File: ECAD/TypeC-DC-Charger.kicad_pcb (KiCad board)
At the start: 4 copper layers, 48 x 56 mm, 91 parts, among them CON1 XT60-PT-MALE, J1 USB_C_SOCKET_RA_SMD, Q1 CSD18543Q3A, Q2 CSD18543Q3A, Q3 CSD17551Q3A, Q4 CSD17551Q3A, Q5 CSD17579Q3A, Q6 CSD17579Q3A, Q7 CSD17579Q3A, Q8 BC857B, Q9 IRFR9024NTRPBF, U1 LM5175RHF, U2 TPS25741, U3 TPS2514

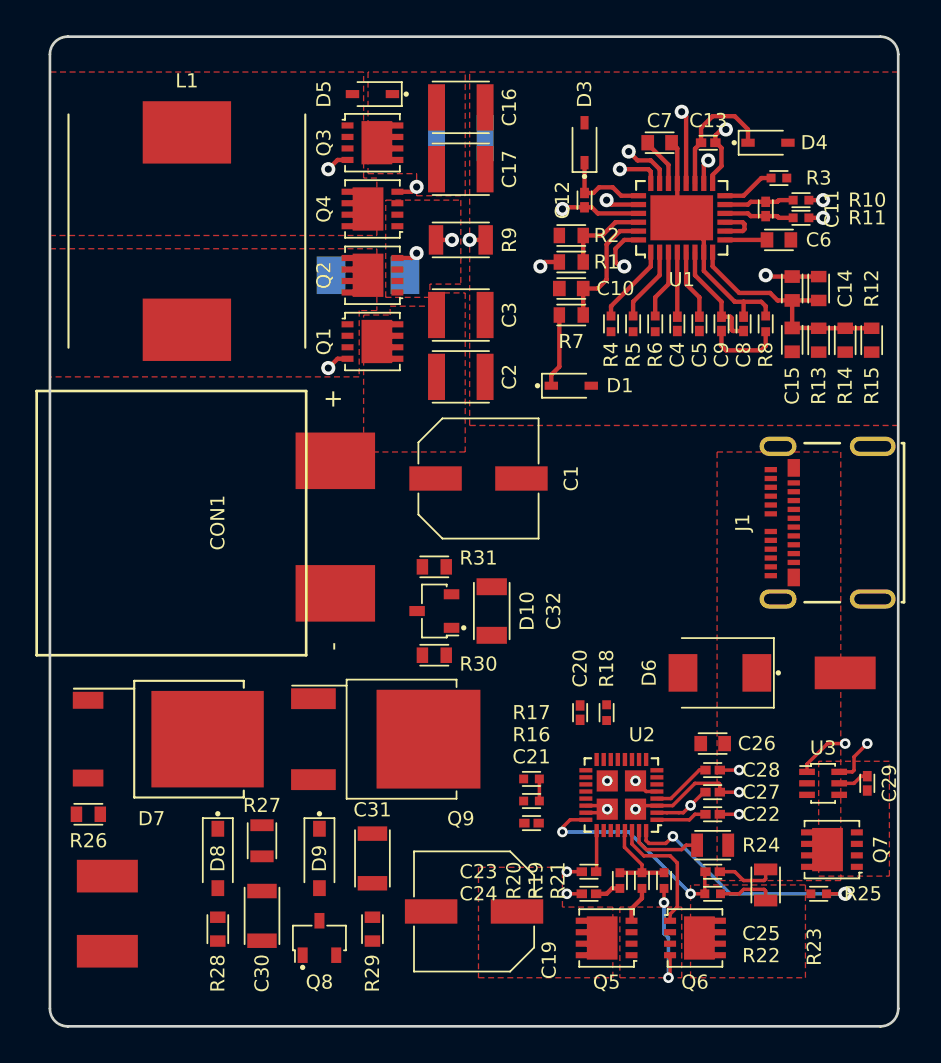
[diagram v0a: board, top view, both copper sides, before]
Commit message: Added dip switch selection to charge settings. PCB placement improvements. Added 3mm led placeholder for indicator led.
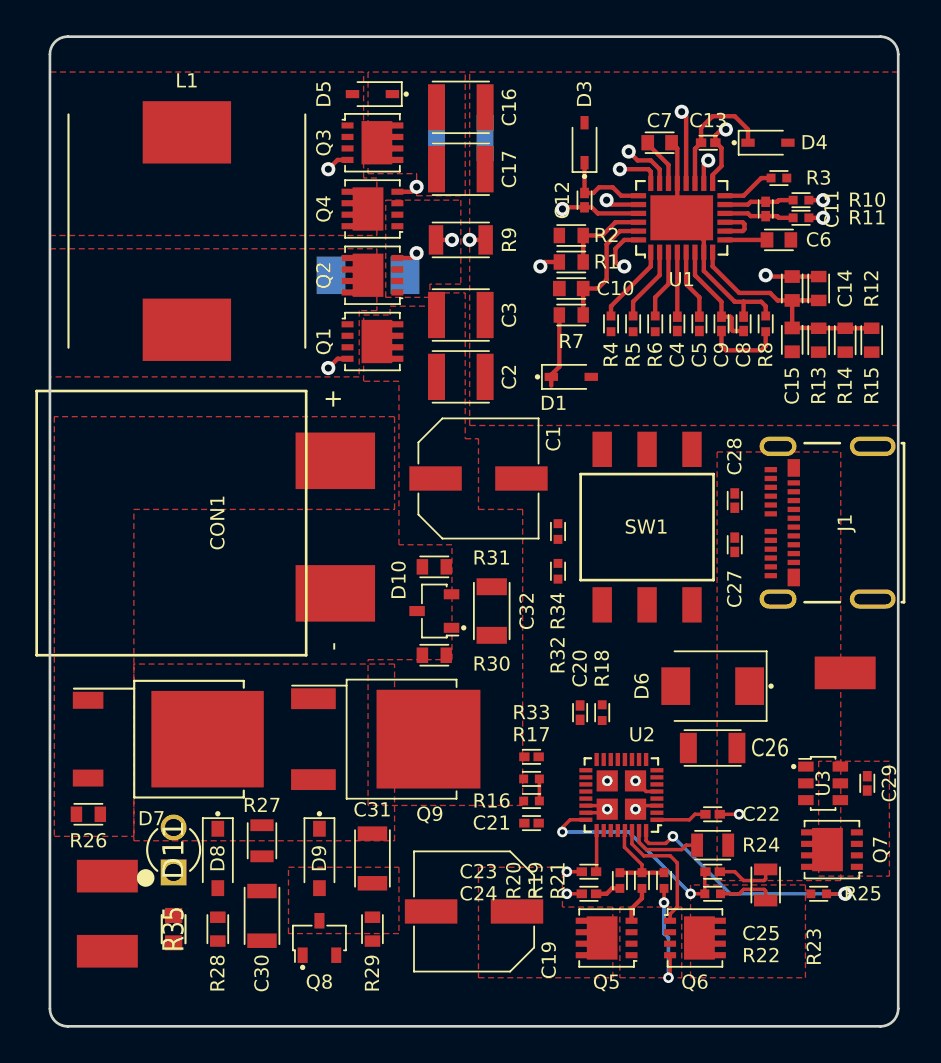
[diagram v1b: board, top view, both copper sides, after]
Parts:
- added D11: LED_RED_3MM_PTH, Applidyne_LED:LEDRD254W40D300H700, F.Cu at (107.0, 96.0)
- added R32: 220K_1005M, Applidyne_Resistor:RESC1005X40L, F.Cu at (128.8, 80.2)
- added R33: 0R_1005M, Applidyne_Capacitor:CAPC1005X60L, F.Cu at (127.2, 90.8)
- added R34: 220K_1005M, Applidyne_Resistor:RESC1005X40L, F.Cu at (128.8, 78.0)
- added R35: 1K00_1608M, Applidyne_Resistor:RESC1608X50N, F.Cu at (107.0, 100.5)
- added SW1: 2.54mm_3xSPST_SMD, Applidyne_Switch:MCEMR-03-T, F.Cu at (131.2, 77.8)
- C26: value 6.8UF_X7R_1608M -> 6.8UF_X7R_3216M; footprint Applidyne_Capacitor:CAPC1608X90L -> Applidyne_Capacitor:CAPC3216X135L
- U3: footprint Applidyne_SOT:SOT23-6P65_210X100L36X22L -> Applidyne_SOT:SOT95P240X110-6L16L
- moved C28 15.3 mm to (138.8, 76.2), turned to 90 degrees
- moved C27 14.1 mm to (138.8, 78.8), turned to 270 degrees
- moved D6 0.85 mm to (137.5, 86.8)
- moved D1 0.50 mm to (129.5, 69.2)
- moved C26 0.25 mm to (137.5, 90.2)
- moved R18 0.25 mm to (131.2, 88.2)
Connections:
- net GDPG renamed Net-(U2-Pad27)
- net Net-(CON1-Pad2) renamed /Connectors/RAW_BATT
- net Net-(R18-Pad2) renamed /USBC Controller/PSEL
- U2 pad 10: /USBC Controller/DVDD -> /USBC Controller/EN12V
- U2 pad 19: /USBC Controller/DVDD -> Net-(R33-Pad2)
- U2 pad 6: /USBC Controller/DVDD -> /USBC Controller/HIPWR
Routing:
- net GND: track 30.3 -> 23.6 mm, vias 11 -> 9
- net CC2: track 3.42 -> 0.00 mm
- net CC1: track 3.23 -> 0.00 mm, vias 1 -> 0
- net D+: track 3.08 -> 0.00 mm, vias 1 -> 0
- net D-: track 2.70 -> 0.00 mm, vias 1 -> 0
- net /Connectors/5V: track 1.76 -> 0.00 mm
- added copper zone on F.Cu, net /Connectors/RAW_BATT
- added copper zone on F.Cu, net Net-(C31-Pad1)
- added copper zone on F.Cu, net Net-(C31-Pad2)

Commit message: Silkscreen text for dip switches, part placement improvements.
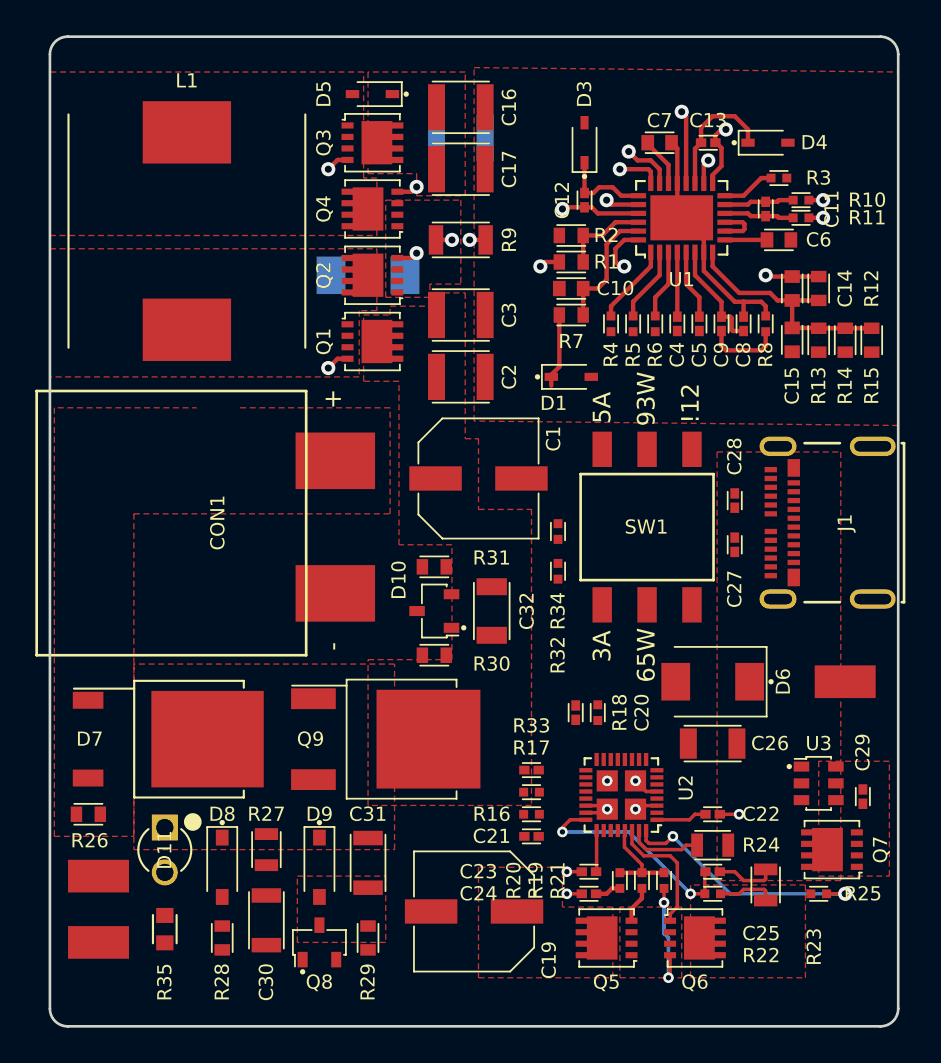
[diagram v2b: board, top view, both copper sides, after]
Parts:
- moved TEST2 4.28 mm to (102.8, 97.5)
- moved TEST5 3.78 mm to (102.8, 101.2)
- moved C29 0.79 mm to (146.0, 93.0)
- moved C21 0.75 mm to (127.2, 95.2)
- moved R16 0.75 mm to (127.2, 94.0)
- moved R17 0.75 mm to (127.2, 92.8)
- moved R33 0.75 mm to (127.2, 91.5)
- moved D8 0.56 mm to (109.8, 97.0)
- moved R27 0.56 mm to (112.2, 96.0)
- moved R28 0.56 mm to (109.8, 101.0)
- moved R29 0.56 mm to (118.0, 101.0)
- moved D11 0.50 mm to (106.5, 96.0), turned to 270 degrees
- moved D9 0.50 mm to (115.2, 97.0)
- moved R35 0.50 mm to (106.5, 100.5)
- moved TEST3 0.50 mm to (145.0, 86.5)
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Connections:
- SW1 pad 3: /USBC Controller/EN12V -> /USBC Controller/PSEL
- SW1 pad 4: GND -> /USBC Controller/DVDD
- SW1 pad 5: /USBC Controller/PSEL -> /USBC Controller/EN12V
- SW1 pad 6: /USBC Controller/DVDD -> GND
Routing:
- net Net-(R16-Pad2): track 1.25 -> 0.00 mm
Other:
- board text added: "!12"
- board text added: "3A"
- board text added: "5A"
- board text added: "65W"
- board text added: "93W"

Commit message: Updated pcb files
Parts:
- moved R25 0.75 mm to (144.2, 98.5), turned to 180 degrees
- moved R26 0.50 mm to (102.7, 94.0)
- moved C29 0.34 mm to (146.0, 92.7)
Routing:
- net VARIABLE_DC: track 10.7 -> 40.9 mm
- net Net-(C31-Pad1): track 0.00 -> 19.9 mm
- net Net-(D8-PadC): track 0.00 -> 18.1 mm
- net /USBC Controller/DVDD: track 0.00 -> 13.0 mm
- net /USBC Controller/EN12V: track 0.00 -> 10.6 mm
- net GND: track 23.6 -> 33.3 mm, vias 9 -> 17
- net Net-(C31-Pad2): track 0.00 -> 8.53 mm, vias 0 -> 2
- net Net-(Q9-Pad1): track 0.00 -> 8.13 mm
- net /USBC Controller/HIPWR: track 0.00 -> 4.44 mm
- net Net-(R16-Pad2): track 0.00 -> 4.41 mm
- net Net-(C32-Pad2): track 0.00 -> 4.13 mm
- net Net-(C21-Pad1): track 0.00 -> 3.95 mm
- net Net-(D11-PadA): track 0.00 -> 2.43 mm
- net G5V: track 14.5 -> 12.2 mm
- net Net-(C30-Pad1): track 0.00 -> 1.72 mm
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- added copper zone on B.Cu, net SW1
- added copper zone on B.Cu, net SW2
